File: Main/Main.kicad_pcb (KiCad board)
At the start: 2 copper layers, 81.3 x 61 mm, 76 parts, among them J1 Conn_02x16_Odd_Even, J2 TYPE-C 6P, Q3 S9013 J3(RANGE:200-350), SW2 SS-12D11G3R, U1 BQ24074RGT, U2 DRV8833PW, U3 HUSB237-AA001-DN06R, U4 RT9742GGJ5, U5 RT9742GGJ5, U6 INA219AxDCN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

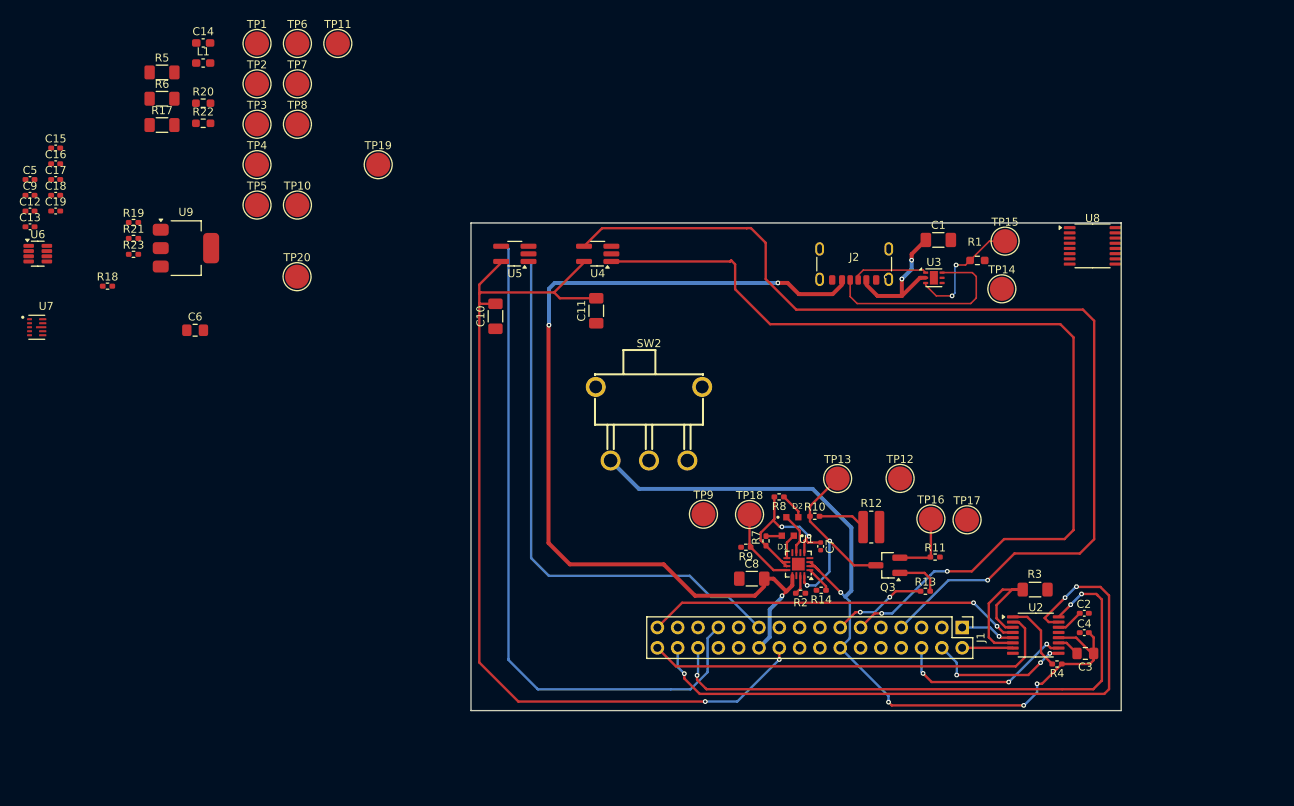
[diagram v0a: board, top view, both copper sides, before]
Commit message: connected other motor
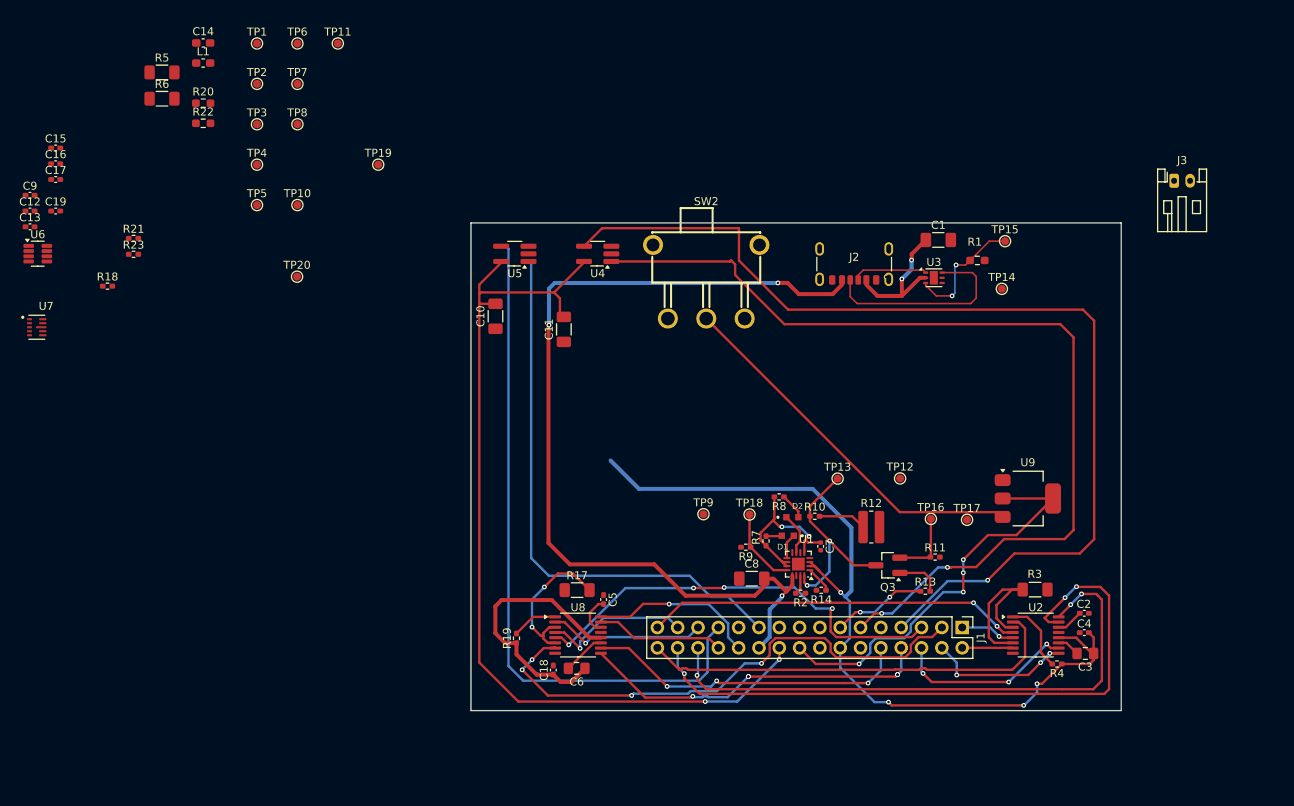
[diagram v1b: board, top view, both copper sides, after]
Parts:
- added J3: Conn_01x02, Connector_JST:JST_PH_S2B-PH-K_1x02_P2.00mm_Horizontal, F.Cu at (181.9, 45.5)
- TP1, TP10, TP11, TP12, TP13, TP14, TP15, TP16, TP17, TP18, TP19, TP2, TP20, TP3, TP4, TP5, TP6, TP7, TP8, TP9: footprint TestPoint:TestPoint_Pad_D3.0mm -> TestPoint:TestPoint_Pad_D1.0mm
- moved U9 109.8 mm to (163.6, 85.2)
- moved C5 88.9 mm to (110.6, 97.9), turned to -90 degrees
- moved C18 86.0 mm to (104.3, 106.7), turned to 90 degrees
- moved U8 80.6 mm to (107.4, 102.3)
- moved R17 77.9 mm to (107.2, 96.7)
- moved R19 70.7 mm to (99.7, 102.7), turned to 90 degrees
- moved C6 63.7 mm to (107.2, 106.5), turned to 180 degrees
- moved SW2 19.1 mm to (123.4, 58.2)
- moved C11 4.67 mm to (105.6, 64.1)
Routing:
- net /Motor4_A_OUT: track 0.00 -> 66.7 mm, vias 0 -> 4
- net /Motor4_B_OUT: track 0.00 -> 54.2 mm, vias 0 -> 4
- net /3V3 Out: track 0.00 -> 51.1 mm, vias 0 -> 4
- net /switch: track 0.00 -> 47.3 mm
- net /MOTOR4_CTRL1: track 0.00 -> 44.4 mm, vias 0 -> 5
- net /MOTOR4_CTRL2: track 0.00 -> 40.9 mm, vias 0 -> 3
- net /Battery: track 104.3 -> 139.4 mm
- net /MOTOR3_CTRL1: track 0.00 -> 21.2 mm, vias 0 -> 1
- net /MOTOR3_A_OUT: track 0.00 -> 19.8 mm, vias 0 -> 1
- net Net-(U8-AISEN): track 0.00 -> 19.0 mm, vias 0 -> 2
- net /MOTOR3_B_OUT: track 0.00 -> 18.7 mm, vias 0 -> 1
- net /MOTOR3_CTRL2: track 0.00 -> 16.0 mm
- net Net-(U8-~{SLEEP}): track 0.00 -> 5.69 mm
- net Net-(U8-VCP): track 0.00 -> 5.39 mm
- net Net-(U8-VINT): track 0.00 -> 4.99 mm
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
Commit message: Poured Ground and connected all PCB items
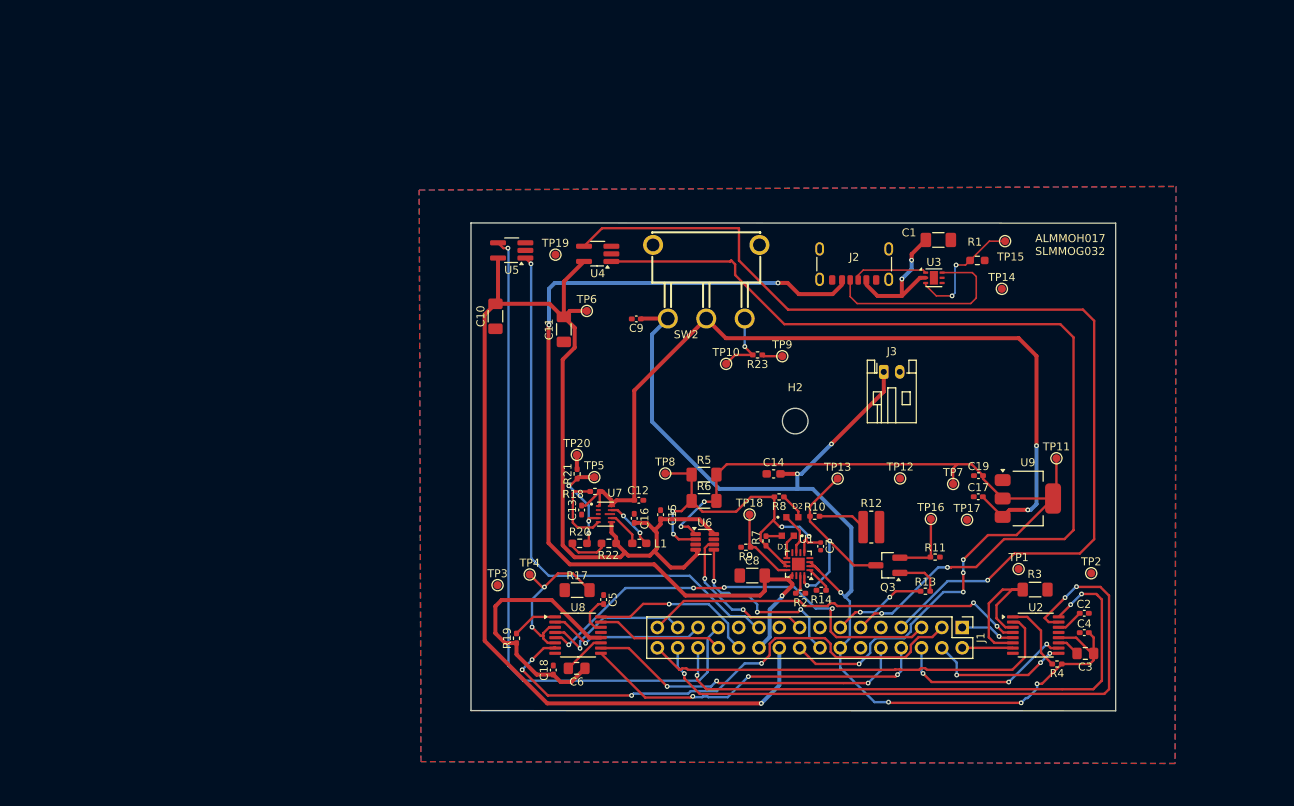
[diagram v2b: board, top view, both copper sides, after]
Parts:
- added H2: MountingHole, MountingHole:MountingHole_3.2mm_M3, F.Cu at (134.5, 75.6)
- moved C17 122.0 mm to (157.4, 85.0)
- moved TP2 120.9 mm to (171.5, 94.6)
- moved C19 120.0 mm to (157.4, 82.4)
- moved TP1 115.7 mm to (162.4, 94.1)
- moved TP11 103.7 mm to (167.2, 80.2)
- moved TP7 96.0 mm to (154.2, 83.4)
- moved U6 90.8 mm to (123.2, 90.7)
- moved C14 89.4 mm to (131.8, 82.2)
- moved C15 88.4 mm to (117.7, 87.3), turned to 90 degrees
- moved C16 84.8 mm to (114.4, 87.7), turned to 90 degrees
- moved R5 84.4 mm to (123.1, 82.3)
- moved R6 84.4 mm to (123.1, 85.5)
- moved C12 84.3 mm to (115.0, 85.5), turned to 180 degrees
- moved L1 81.1 mm to (115.0, 90.8)
- moved R23 79.0 mm to (129.8, 67.3), turned to 180 degrees
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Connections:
- R5 pad 1: /Load -> /VOUT
- R6 pad 1: /Load -> /VOUT
- TP8 pad 1: /Load -> /VOUT
- U6 pad 2: /Load -> /VOUT
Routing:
- net /5V Out: track 114.7 -> 183.9 mm, vias 2 -> 1
- net /switch: track 47.3 -> 107.3 mm, vias 0 -> 2
- net /3V3 Out: track 51.1 -> 108.7 mm, vias 4 -> 6
- net /Battery: track 139.4 -> 174.3 mm, vias 4 -> 6
- net /VOUT: track 21.1 -> 48.3 mm, vias 2 -> 4
- net /I2C1_SCL: track 0.00 -> 23.2 mm, vias 0 -> 3
- net /I2C1_SDA: track 0.00 -> 19.8 mm, vias 0 -> 2
- net Net-(U7-FB): track 0.00 -> 13.8 mm, vias 0 -> 3
- net Net-(U7-PG): track 0.00 -> 9.66 mm
- net Net-(R23-Pad2): track 0.00 -> 8.76 mm, vias 0 -> 1
- net Net-(U7-L1): track 0.00 -> 6.45 mm, vias 0 -> 2
- net Net-(R20-Pad1): track 0.00 -> 5.12 mm
- net Net-(U7-L2): track 0.00 -> 4.55 mm
- net GND: track 0.08 -> 4.47 mm
- net Net-(U8-AISEN): track 19.0 -> 21.5 mm
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- added copper zone on B.Cu, net GND
- added copper zone on F.Cu, net GND
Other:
- board size 81.3 x 61 mm -> 80.6 x 61 mm
- board text added: "ALMMOH017 SLMMOG032"

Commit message: Using a new Motor Driver bc old one no stock
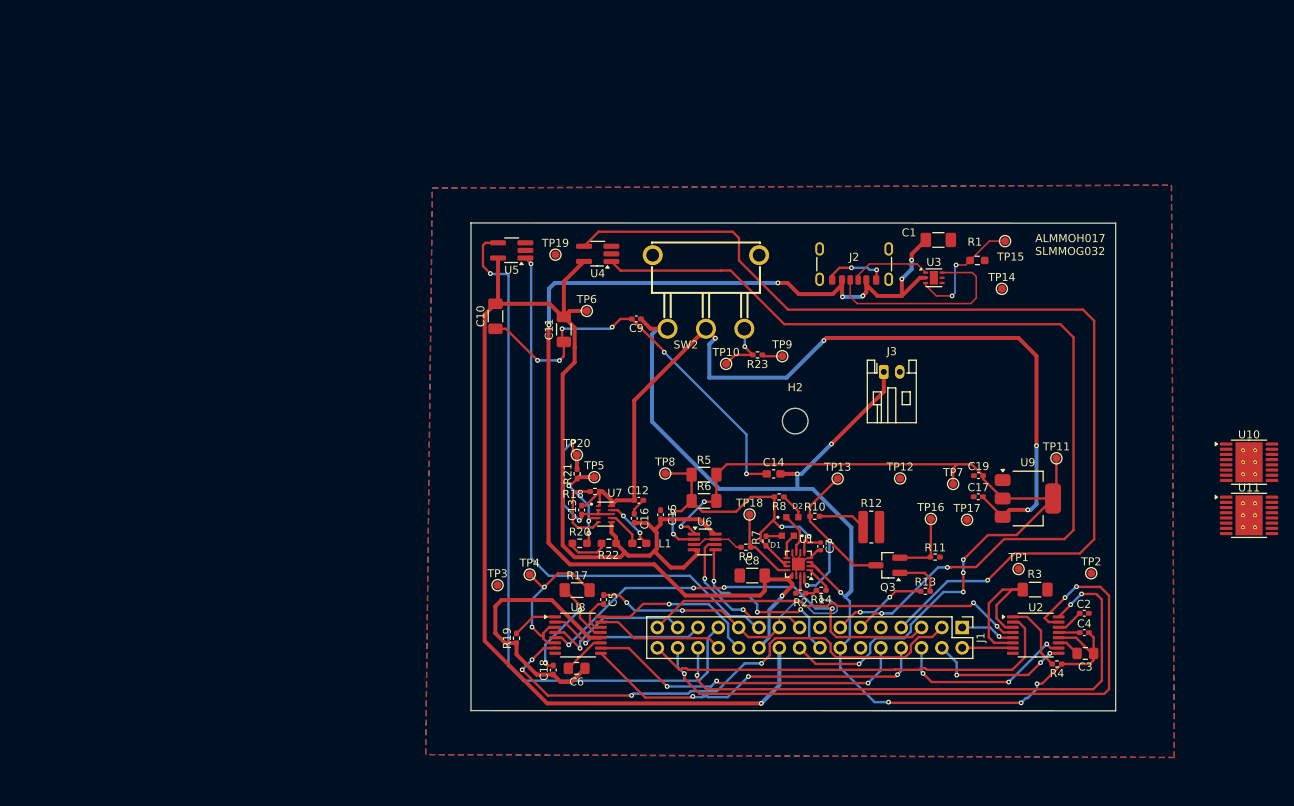
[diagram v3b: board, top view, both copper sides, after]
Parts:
- added U10: DRV8833PWP, Package_SO:HTSSOP-16-1EP_4.4x5mm_P0.65mm_EP3.4x5mm_Mask2.46x2.31mm_ThermalVias, F.Cu at (191.2, 80.7)
- added U11: DRV8833PWP, Package_SO:HTSSOP-16-1EP_4.4x5mm_P0.65mm_EP3.4x5mm_Mask2.46x2.31mm_ThermalVias, F.Cu at (191.2, 87.4)
- U6: footprint Package_TO_SOT_SMD:SOT-23-8 -> Package_TO_SOT_SMD:SOT-23-8_Handsoldering
- moved SW2 1.28 mm to (123.3, 59.4)
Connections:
- C2 pad 2: Net-(U2-VINT) -> Net-(U11-VINT)
- C3 pad 2: Net-(U2-VCP) -> Net-(U11-VCP)
- C5 pad 2: Net-(U8-VINT) -> Net-(U10-VINT)
- C6 pad 2: Net-(U8-VCP) -> Net-(U10-VCP)
- R17 pad 2: Net-(U8-AISEN) -> Net-(U10-AISEN)
- R19 pad 2: Net-(U8-~{SLEEP}) -> Net-(U10-~{SLEEP})
- R3 pad 2: Net-(U2-AISEN) -> Net-(U11-AISEN)
- R4 pad 2: Net-(U2-~{SLEEP}) -> Net-(U11-~{SLEEP})
- TP1 pad 1: Net-(U2-AISEN) -> Net-(U11-AISEN)
- TP4 pad 1: Net-(U8-AISEN) -> Net-(U10-AISEN)
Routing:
- net GND: track 4.47 -> 159.7 mm, vias 0 -> 15
- net /High Voltage (9V): track 133.9 -> 141.4 mm, vias 5 -> 7
- net /switch: track 107.3 -> 113.6 mm, vias 2 -> 4
- net /CTRL_EXT_LOAD1: track 86.0 -> 89.3 mm
- net Net-(R23-Pad2): track 8.76 -> 7.53 mm
- net /CTRL_EXT_LOAD2: track 127.9 -> 126.8 mm
- net /Battery: track 174.3 -> 175.2 mm
- net /EXT_LOAD2_OUT: track 118.3 -> 117.5 mm
- net Net-(J2-CC1): track 9.43 -> 10.2 mm

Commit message: NO ERRORS
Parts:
- removed U2, U8: DRV8833PW, Package_SO:TSSOP-16_4.4x5mm_P0.65mm
- U10, U11: footprint Package_SO:HTSSOP-16-1EP_4.4x5mm_P0.65mm_EP3.4x5mm_Mask2.46x2.31mm_ThermalVias -> Package_SO:HTSSOP-16-1EP_4.4x5mm_P0.65mm_EP3.4x5mm_Mask2.46x2.31mm
- moved U10 87.1 mm to (106.9, 102.3)
- moved U11 30.4 mm to (164.8, 102.3)
- moved C3 0.56 mm to (171.3, 104.6)
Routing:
- net /Battery: track 175.2 -> 227.3 mm, vias 6 -> 11
- net GND: track 159.7 -> 202.7 mm, vias 15 -> 17
- net Net-(U11-AISEN): track 0.00 -> 23.9 mm
- net Net-(U10-AISEN): track 0.00 -> 23.9 mm, vias 0 -> 2
- net Net-(U8-AISEN): track 21.5 -> 0.00 mm, vias 2 -> 0
- net Net-(U2-AISEN): track 20.7 -> 0.00 mm
- net Net-(U11-~{SLEEP}): track 0.00 -> 13.6 mm, vias 0 -> 2
- net Net-(U2-~{SLEEP}): track 8.98 -> 0.00 mm
- net /MOTOR3_A_OUT: track 19.8 -> 28.7 mm, vias 1 -> 4
- net Net-(U10-VCP): track 0.00 -> 8.29 mm, vias 0 -> 2
- net Net-(U10-VINT): track 0.00 -> 7.30 mm, vias 0 -> 2
- net /MOTOR3_B_OUT: track 18.7 -> 25.4 mm
- net /Motor4_B_OUT: track 54.2 -> 60.8 mm
- net Net-(U8-~{SLEEP}): track 5.69 -> 0.00 mm
- net Net-(U10-~{SLEEP}): track 0.00 -> 5.64 mm
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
